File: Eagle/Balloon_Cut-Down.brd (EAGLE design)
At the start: 42.5 x 58.4 mm, 64 parts, among them Q1 DMG3415U-7, U1 MCP111T-240E/TT, U2 SPX3819-3.3, U3 MPM3610, U4 74AHCT1G125DBV, U5 ATSAMD21G18_QFN, X1 32.768

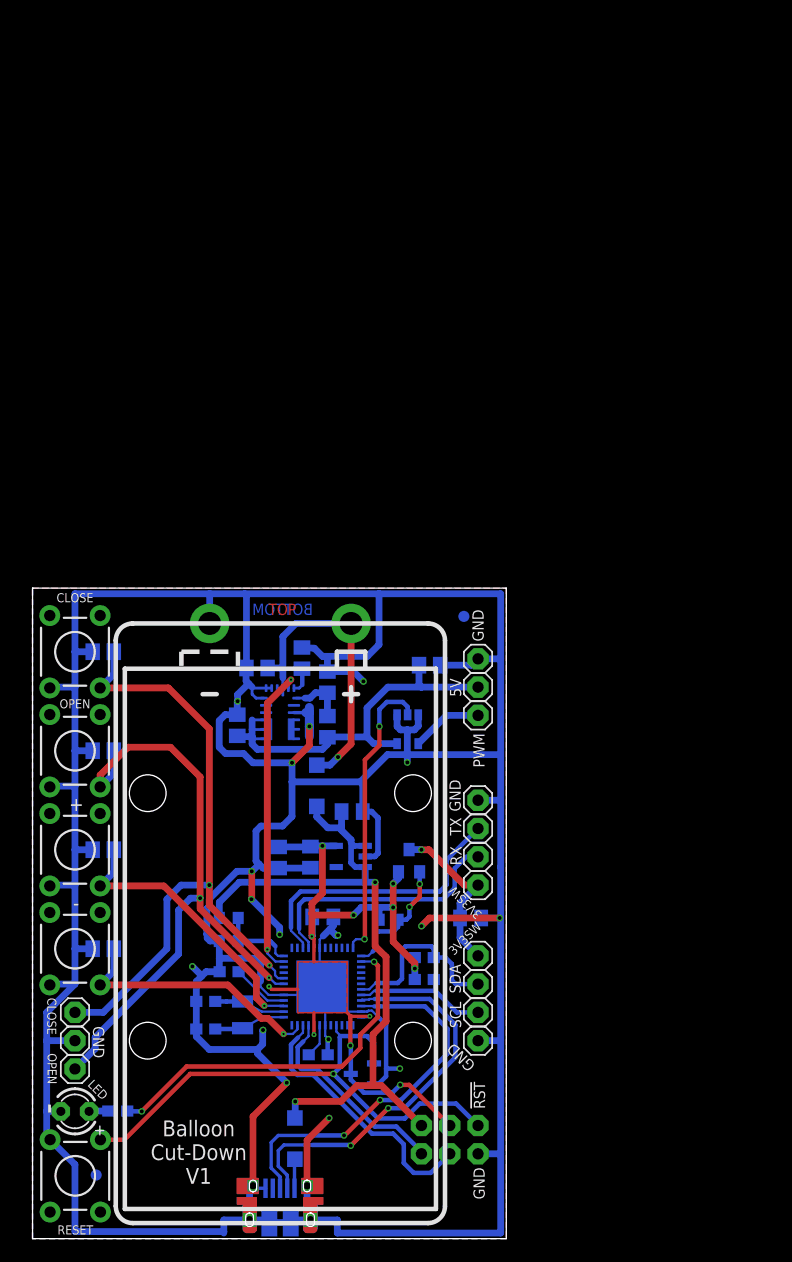
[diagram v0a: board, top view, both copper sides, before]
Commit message: Major update for the V3 PCB
Major update for the V3 PCB: the cut-down is now based on the eRIC4 or eRIC9 radio controller and can be triggered by radio; a u-blox CAM-M8Q provides altitude information; the Shark and Servo are now mounted directly on the PCB instead of carbon fibre. The V1 files are in the Archive folder.
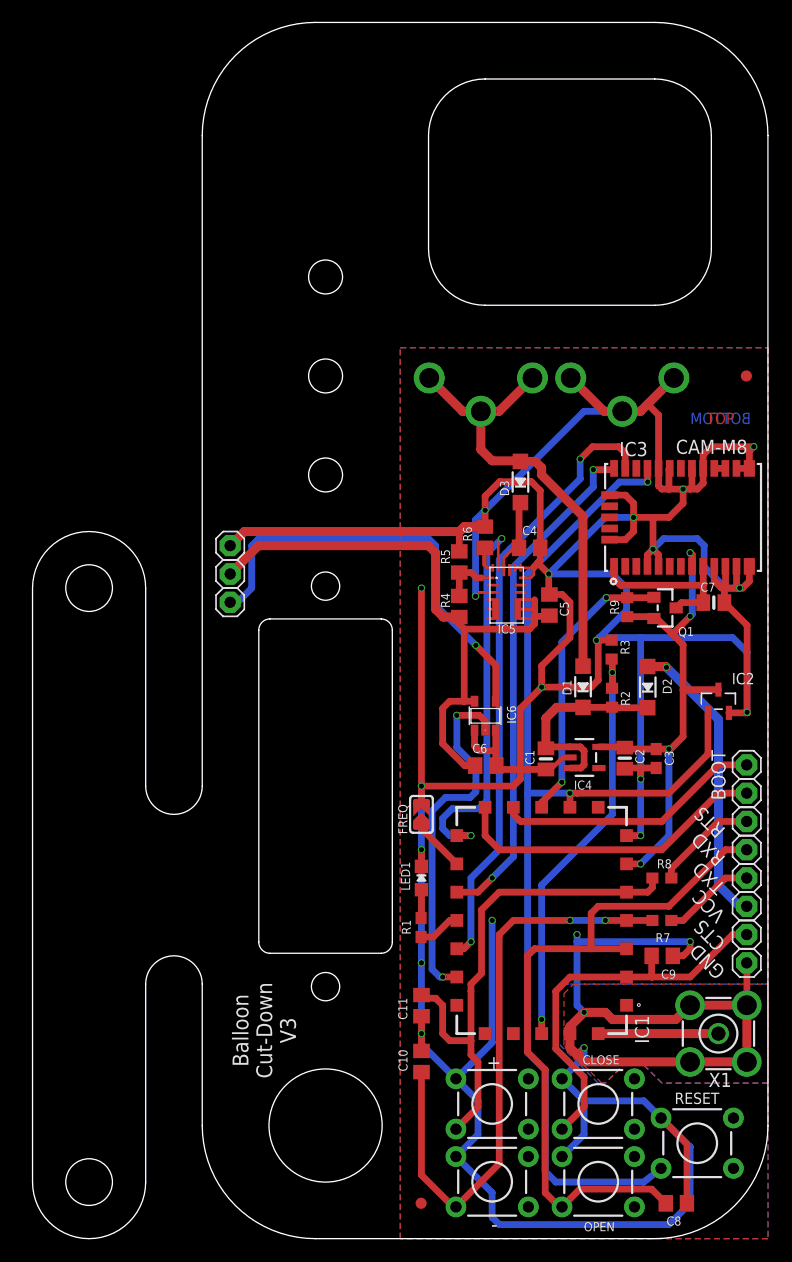
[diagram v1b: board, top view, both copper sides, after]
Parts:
- removed !RST, 3V3, 3V3SW1, 3V3SW2, CLOSE, GND3, GND4, GND5, OPEN, RX, SCL, SDA, SWCLK, SWDIO, TX, VBUS: (no value), adafruit:1X01
- removed C12: 0.1uF, microbuilder:0805-NO
- removed C13, C14, C15, C16: 10nF, rcl:C0805
- removed CON1: (no value), microbuilder:FCI_10103594
- removed LED: RED, adafruit:LED3MM
- removed S5: SWITCH-MOMENTARY-2PTH, SparkFun-Electromechanical:TACTILE-PTH
- removed U1: MCP111T-240E/TT, Microchip-MCP11:SOT95P237X112-3N
- removed U2: SPX3819-3.3, microbuilder:SOT23-5
- removed U3: MPM3610, IntegratedCircuits:QFN-20
- removed U4: 74AHCT1G125DBV, 74xx-little-us:SOT23-5
- removed U5: ATSAMD21G18_QFN, microbuilder:TQFN48_7MM
- added BOOT1, BOOT2, CTS, RTS, RXD, TXD, VCC: (no value), adafruit:1X01
- added D3: MBR120, microbuilder:SOD-123
- added FREQ: (no value), microbuilder:SOLDERJUMPER_ARROW_NOPASTE
- added IC1: ERIC9-FCC, SamacSys_Parts:ERIC4
- added IC2: MCP111T-240E/TT, Microchip-MCP11:SOT95P237X112-3N
- added IC3: CAM-M8, ubloxLib:CAM-M8
- added IC4: SPX3819-3.3, microbuilder:SOT23-5
- added IC5: MPM3610, IntegratedCircuits:QFN-20
- added IC6: 74AHCT1G125DBV, 74xx-little-us:SOT23-5
- added LED1: RED, microbuilder:CHIPLED_0805_NOOUTLINE
- added RESET: SWITCH-MOMENTARY-2PTH, SparkFun-Electromechanical:TACTILE-PTH
- BAT: device SparkFun-Electromechanical:BATTERY-9V-KEYSTONE1294 -> SparkFun-Electromechanical:BATTERY-9V-KEYSTONE-593-594
- C1: value 1uF -> 10µF; device microbuilder:0603-NO -> microbuilder:0805-NO
- C10: value 22uF -> 1nF
- C2: value 12pF -> 10µF; device microbuilder:0603-NO -> microbuilder:0805-NO
- C3: value 12pF -> 100nF
- C4: value 10µF -> 10uF; device microbuilder:0805-NO -> rcl:C0805
- C5: device microbuilder:0805-NO -> rcl:C0805
- C6: value 10µF -> 10nF; device microbuilder:0805-NO -> rcl:C0805
- C7: value 10nF -> 0.1uF; device rcl:C0805 -> microbuilder:0805-NO
- C8: value 1uF -> 10nF; device microbuilder:0603-NO -> rcl:C0805
- C9: value 10uF -> 10nF
- R1, R7, R8: value 2.2K -> 1K
- X1: value 32.768 -> BU-SMA-V; device adafruit2:XTAL3215 -> con-coax:BU-SMA-V
- moved S3 60.6 mm to (41.3, 5.11), turned to 0 degrees
- moved S2 56.7 mm to (50.8, 12.1), turned to 0 degrees
- moved D2 51.5 mm to (55.2, 49.5), flipped to the top, turned to 90 degrees
- moved S1 47.0 mm to (50.8, 5.11), turned to 0 degrees
- moved C3 46.0 mm to (56.0, 43.1), flipped to the top, turned to 270 degrees
- moved C7 45.3 mm to (61.2, 57.1), flipped to the top, turned to 0 degrees
- moved C8 45.2 mm to (57.8, 3.17), flipped to the top, turned to 180 degrees
- moved C2 44.8 mm to (53.2, 43.1), flipped to the top, turned to 270 degrees
- moved C9 44.6 mm to (56.5, 25.4), flipped to the top, turned to 180 degrees
- moved S4 43.9 mm to (41.3, 12.1), turned to 0 degrees
- moved R3 43.2 mm to (52.0, 52.9), flipped to the top, turned to 270 degrees
- moved X1 42.8 mm to (61.6, 18.4), flipped to the top, turned to 0 degrees
- moved R2 39.7 mm to (52.0, 48.6), flipped to the top, turned to 270 degrees
- moved R9 35.3 mm to (53.4, 56.7), flipped to the top, turned to 90 degrees
- moved C5 34.6 mm to (46.4, 56.9), flipped to the top, turned to 90 degrees
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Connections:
- removed net A0: C15.2, S4.3, U5.3
- removed net A1: C13.2, OPEN.1, S2.3, U5.7
- removed net A2: C14.2, CLOSE.1, S3.3, U5.8
- removed net A3: U5.9
- removed net A4: U5.10
- removed net A5: C16.2, S5.3, U5.47
- removed net AREF: C8.1, U5.4
- removed net D+: CON1.D+, U5.34
- removed net D-: CON1.D-, U5.33
- removed net D0: RX.1, U5.16
- removed net D1: TX.1, U5.15
- removed net D10: U5.27
- removed net D11: Q1.1, R9.2, U5.25
- removed net D12: U5.28
- removed net D13: R1.1, U5.26
- removed net D2: U5.23
- removed net D3: U5.14
- removed net D5: U4.2, U5.24
- removed net D6: U5.29
- removed net D7: U5.30
- removed net D8: U3.17, U5.11
- removed net D9: R2.1, R3.2, U5.12
- removed net MISO: U5.21
- removed net MOSI: U5.19
- removed net N$16: CON1.VBUS, D2.A
- removed net N$5: C2.1, U5.1, X1.P$1
- removed net N$7: C3.1, U5.2, X1.P$2
- removed net SCK: U5.20
- removed net SCL: R7.2, SCL.1, U5.32
- removed net SDA: R8.2, SDA.1, U5.31
- removed net SD_CS: U5.13
- removed net SWCLK: SWCLK.1, U5.45
- removed net SWDIO: SWDIO.1, U5.46
- removed net VDDCORE1: C1.1, U5.43
- new net CTS: C9.2, CTS.1, IC1.2, S2.3
- new net FREQ: FREQ.1, IC1.14
- new net N$1: R7.1, TXD.1
- new net N$2: IC3.16, IC3.17
- new net N$4: R8.1, RTS.1
- new net N$6: C4.1, D3.C, IC5.16
- new net N$9: D2.A, VCC.1
- new net PIN10: IC1.10, Q1.1, R9.2
- new net PIN11: BOOT1.1, IC1.11
- new net PIN12: BOOT2.1, IC1.12
- new net PIN13: IC1.13, IC5.17
- new net PIN15: IC1.15, IC3.26
- new net PIN16: IC1.16, R1.1
- new net PIN17: IC1.17, IC3.25
- new net PIN18: IC1.18, IC6.2
- new net PIN19: IC1.19
- new net PIN20: IC1.20
- new net PIN21: IC1.21
- new net PIN22: IC1.22, R2.1, R3.2
- new net RF: IC1.24, X1.1
- new net RTS: C11.2, IC1.5, R8.2, S4.3
- new net RXD: C8.2, IC1.3, RXD.1, S1.3
- new net TXD: C10.2, IC1.4, R7.2, S3.3
- net !RESET: now also IC1.9, IC2.1, IC3.23, RESET.3; no longer !RST.1, S1.1, U1.1, U5.40
- net +3V3: now also C2.1, C3.1, IC1.6, IC2.3, IC3.8, IC4.5; no longer 3V3.1, C5.1, C6.1, C7.1, R7.1, R8.1, U1.3, U2.5, U5.17, U5.36, U5.44, U5.6
- net +5V: now also C5.1, C6.1, IC5.20, IC5.7, IC5.8, IC5.9, IC6.5; no longer C10.1, C11.1, U3.20, U3.7, U3.8, U3.9, U4.5
- net 3V3SW: now also C7.1, IC3.1, IC3.9; no longer 3V3SW1.1, 3V3SW2.1, C12.1
- net GND: now also BAT.GND1, BAT.GND2, C10.1, C11.1, C8.1, C9.1, FREQ.2, IC1.23, IC1.7, IC2.2, IC3.10, IC3.11, IC3.12, IC3.13, IC3.14, IC3.15, IC3.18, IC3.19, IC3.21, IC3.22, IC3.27, IC3.31, IC3.4, IC3.5, IC4.2, IC5.12, IC5.13, IC5.14, IC5.3, IC6.1, IC6.3, LED1.C, RESET.1, S1.1, X1.2, X1.3, X1.4, X1.5; no longer C10.2, C11.2, C12.2, C13.1, C14.1, C15.1, C16.1, C8.2, C9.2, CON1.BASE@1, CON1.BASE@2, CON1.GND, CON1.SPRT@1, CON1.SPRT@2, CON1.SPRT@3, CON1.SPRT@4, GND3.1, GND4.1, GND5.1, LED.K, S1.3, S5.1, U1.2, U2.2, U3.12, U3.13, U3.14, U3.3, U4.1, U4.3, U5.18, U5.35, U5.42, U5.5, U5.THERMAL
- net N$26: now also IC5.1; no longer U3.1
- net N$29: now also IC5.18; no longer U3.18
- net N$3: now also LED1.A; no longer LED.A
- net PWM: now also IC6.4; no longer U4.4
- net VBAT: now also BAT.PWR1, BAT.PWR2, D3.A; no longer C9.1, U3.16
- net VBUS: now also C1.1, IC4.1, IC4.3; no longer C4.1, U2.1, U2.3, VBUS.1
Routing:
- net RXD: track 0.00 -> 63.1 mm
- net A2: track 60.0 -> 0.00 mm, vias 2 -> 0
- net A1: track 58.6 -> 0.00 mm, vias 2 -> 0
- net PIN17: track 0.00 -> 55.0 mm, vias 0 -> 2
- net !RESET: track 49.3 -> 103.6 mm, vias 1 -> 2
- net TXD: track 0.00 -> 53.9 mm, vias 0 -> 2
- net PIN15: track 0.00 -> 46.0 mm, vias 0 -> 2
- net RTS: track 0.00 -> 45.8 mm
- net VBUS: track 63.0 -> 18.6 mm, vias 2 -> 0
- net GND: track 450.1 -> 489.7 mm, vias 17 -> 23
- net +3V3: track 85.6 -> 47.7 mm, vias 11 -> 4
- net PIN22: track 0.00 -> 37.7 mm, vias 0 -> 2
- net PIN13: track 0.00 -> 36.5 mm, vias 0 -> 2
- net D-: track 35.5 -> 0.00 mm, vias 2 -> 0
- net CTS: track 0.00 -> 35.4 mm
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- removed copper zone on layer 1, net +3V3
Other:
- board size 42.5 x 58.4 mm -> 66 x 109.2 mm
- board text added: "BOOT"
- board text added: "Balloon Cut-Down V3"
- board text removed: "!RST"
- board text removed: "3V3SW"
- board text removed: "Balloon Cut-Down V1"
- board text removed: "RESET"
